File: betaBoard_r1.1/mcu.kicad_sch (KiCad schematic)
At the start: 27 parts, among them SW1 C26638, SW2 C26638, U2 W25Q128JVSIQ, U3 RP2040, Y1 X322512MSB4SI

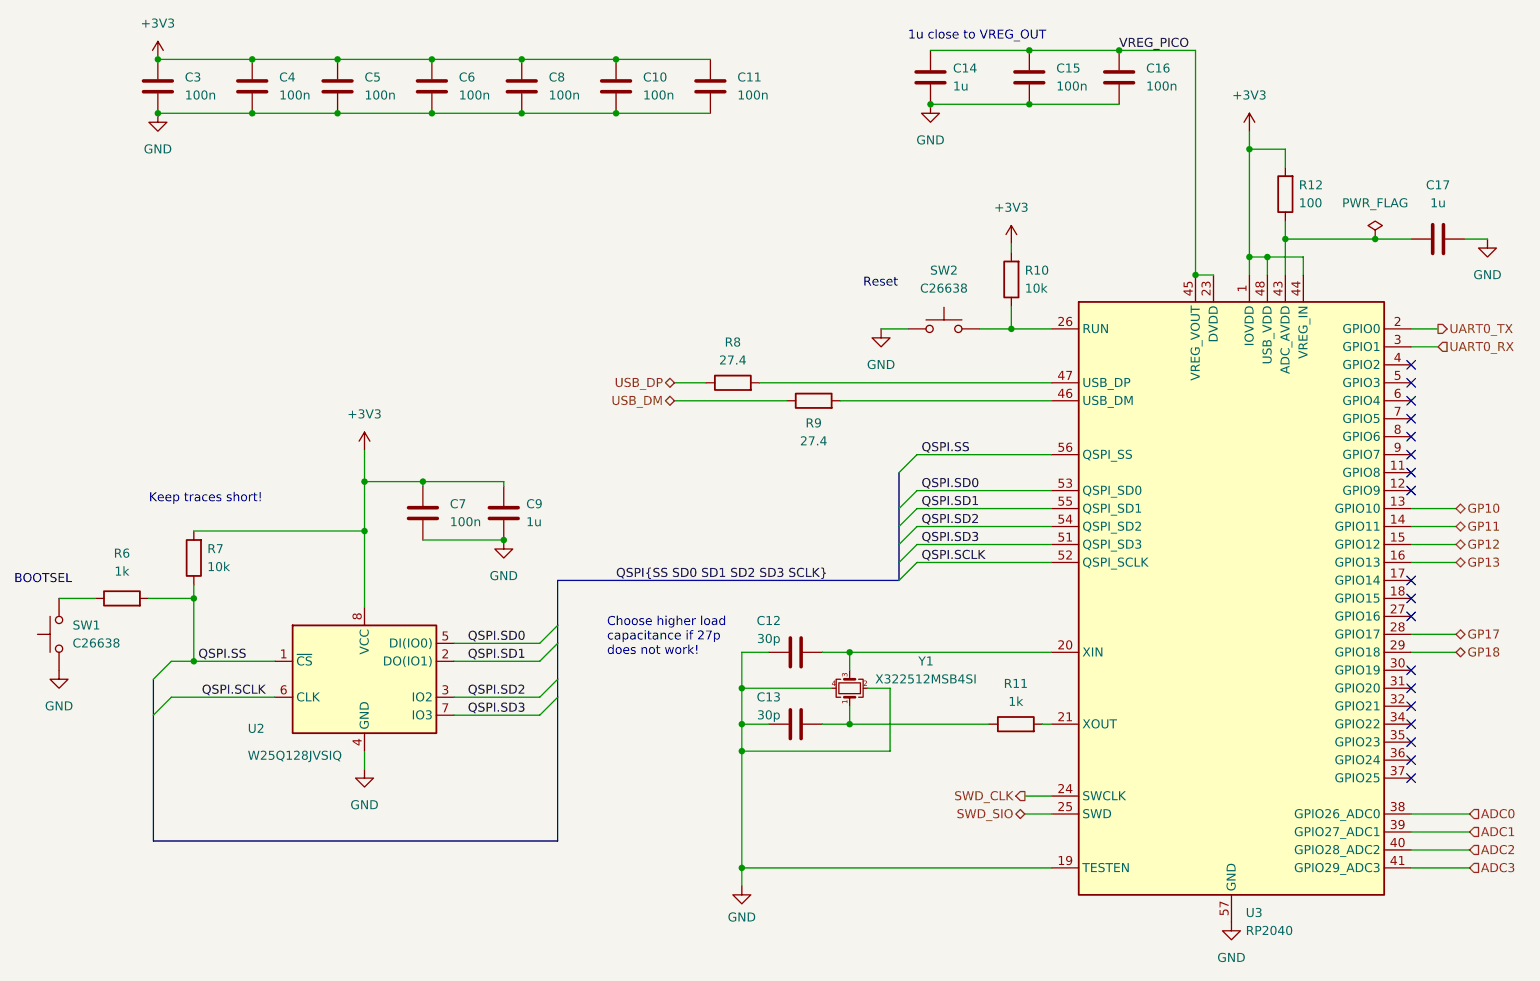
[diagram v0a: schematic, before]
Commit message: move all hardware files to one folder
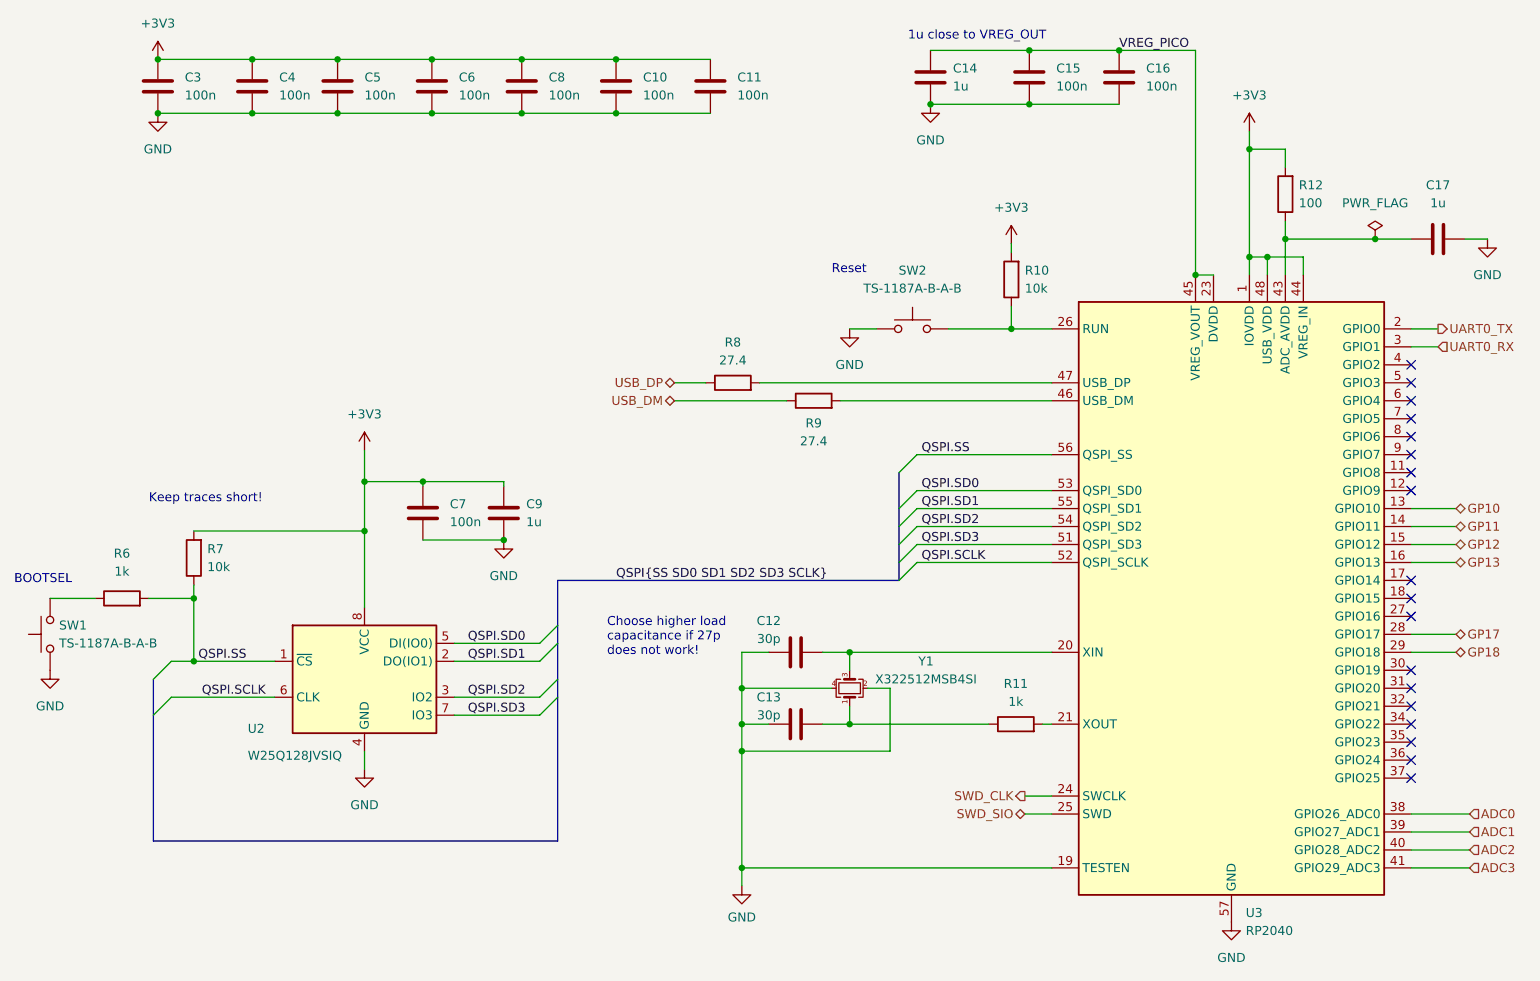
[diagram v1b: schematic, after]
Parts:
- SW1, SW2: value C26638 -> TS-1187A-B-A-B
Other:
- moved on the sheet: SW1, SW2
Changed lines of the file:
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@@
     (title "Beta Board")
     (date "2023-12-28")
-    (rev "R1.0")
+    (rev "R1.1")
     (company "Tim Kuhlbusch")
     (comment 1 "Beta radiation detector")
@@
     (stroke (width 0) (type default))
   )
-  (wire (pts (xy 141.605 71.12) (xy 145.415 71.12))
+  (wire (pts (xy 137.16 71.12) (xy 140.97 71.12))
     (stroke (width 0) (type default))
   )
@@
     (stroke (width 0) (type default))
   )
-  (wire (pts (xy 155.575 71.12) (xy 160.02 71.12))
+  (wire (pts (xy 151.13 71.12) (xy 160.02 71.12))
     (stroke (width 0) (type default))
   )
@@
     (stroke (width 0) (type default))
   )
-  (wire (pts (xy 25.4 109.22) (xy 30.48 109.22))
+  (wire (pts (xy 24.13 109.22) (xy 30.48 109.22))
     (stroke (width 0) (type default))
   )
@@
     (effects (font (size 1.27 1.27)) (justify left bottom))
   )
-  (text "Reset\n" (at 139.065 65.405 0)
+  (text "Reset\n" (at 134.62 63.5 0)
     (effects (font (size 1.27 1.27)) (justify left bottom))
   )
@@
     )
   )
-  (symbol (lib_id "power:GND") (at 141.605 71.12 0) (unit 1)
-    (in_bom yes) (on_board yes) (dnp no) (fields_autoplaced)
-    (property "Reference" "#PWR023" (at 141.605 77.47 0)
-      (effects (font (size 1.27 1.27)) hide)
-    )
-    (property "Value" "GND" (at 141.605 76.2 0)
-      (effects (font (size 1.27 1.27)))
-    )
-    (property "Footprint" "" (at 141.605 71.12 0)
-      (effects (font (size 1.27 1.27)) hide)
-    )
-    (property "Datasheet" "" (at 141.605 71.12 0)
+  (symbol (lib_id "power:GND") (at 137.16 71.12 0) (unit 1)
+    (in_bom yes) (on_board yes) (dnp no) (fields_autoplaced)
+    (property "Reference" "#PWR023" (at 137.16 77.47 0)
+      (effects (font (size 1.27 1.27)) hide)
+    )
+    (property "Value" "GND" (at 137.16 76.2 0)
+      (effects (font (size 1.27 1.27)))
+    )
+    (property "Footprint" "" (at 137.16 71.12 0)
+      (effects (font (size 1.27 1.27)) hide)
+    )
+    (property "Datasheet" "" (at 137.16 71.12 0)
       (effects (font (size 1.27 1.27)) hide)
     )
@@
     )
   )
-  (symbol (lib_id "power:GND") (at 25.4 119.38 0) (unit 1)
-    (in_bom yes) (on_board yes) (dnp no) (fields_autoplaced)
-    (property "Reference" "#PWR016" (at 25.4 125.73 0)
-      (effects (font (size 1.27 1.27)) hide)
-    )
-    (property "Value" "GND" (at 25.4 124.46 0)
-      (effects (font (size 1.27 1.27)))
-    )
-    (property "Footprint" "" (at 25.4 119.38 0)
-      (effects (font (size 1.27 1.27)) hide)
-    )
-    (property "Datasheet" "" (at 25.4 119.38 0)
+  (symbol (lib_id "power:GND") (at 24.13 119.38 0) (unit 1)
+    (in_bom yes) (on_board yes) (dnp no) (fields_autoplaced)
+    (property "Reference" "#PWR016" (at 24.13 125.73 0)
+      (effects (font (size 1.27 1.27)) hide)
+    )
+    (property "Value" "GND" (at 24.13 124.46 0)
+      (effects (font (size 1.27 1.27)))
+    )
+    (property "Footprint" "" (at 24.13 119.38 0)
+      (effects (font (size 1.27 1.27)) hide)
+    )
+    (property "Datasheet" "" (at 24.13 119.38 0)
       (effects (font (size 1.27 1.27)) hide)
     )
@@
     )
   )
-  (symbol (lib_id "Switch:SW_Push") (at 150.495 71.12 0) (unit 1)
-    (in_bom yes) (on_board yes) (dnp no) (fields_autoplaced)
-    (property "Reference" "SW2" (at 150.495 62.865 0)
-      (effects (font (size 1.27 1.27)))
-    )
-    (property "Value" "C26638" (at 150.495 65.405 0)
-      (effects (font (size 1.27 1.27)))
-    )
-    (property "Footprint" "betaBoard:TS-1187A-B-A-B" (at 150.495 66.04 0)
-      (effects (font (size 1.27 1.27)) hide)
-    )
-    (property "Datasheet" "~" (at 150.495 66.04 0)
+  (symbol (lib_id "Switch:SW_Push") (at 146.05 71.12 0) (unit 1)
+    (in_bom yes) (on_board yes) (dnp no) (fields_autoplaced)
+    (property "Reference" "SW2" (at 146.05 62.865 0)
+      (effects (font (size 1.27 1.27)))
+    )
+    (property "Value" "TS-1187A-B-A-B" (at 146.05 65.405 0)
+      (effects (font (size 1.27 1.27)))
+    )
+    (property "Footprint" "betaBoard:TS-1187A-B-A-B" (at 146.05 66.04 0)
+      (effects (font (size 1.27 1.27)) hide)
+    )
+    (property "Datasheet" "~" (at 146.05 66.04 0)
       (effects (font (size 1.27 1.27)) hide)
     )
@@
     )
   )
-  (symbol (lib_id "Switch:SW_Push") (at 25.4 114.3 90) (unit 1)
-    (in_bom yes) (on_board yes) (dnp no) (fields_autoplaced)
-    (property "Reference" "SW1" (at 27.305 113.0299 90)
+  (symbol (lib_id "Switch:SW_Push") (at 24.13 114.3 90) (unit 1)
+    (in_bom yes) (on_board yes) (dnp no) (fields_autoplaced)
+    (property "Reference" "SW1" (at 25.4 113.03 90)
       (effects (font (size 1.27 1.27)) (justify right))
     )
-    (property "Value" "C26638" (at 27.305 115.5699 90)
+    (property "Value" "TS-1187A-B-A-B\n" (at 25.4 115.57 90)
       (effects (font (size 1.27 1.27)) (justify right))
     )
-    (property "Footprint" "betaBoard:TS-1187A-B-A-B" (at 20.32 114.3 0)
-      (effects (font (size 1.27 1.27)) hide)
-    )
-    (property "Datasheet" "~" (at 20.32 114.3 0)
-      (effects (font (size 1.27 1.27)) hide)
-    )
+    (property "Footprint" "betaBoard:TS-1187A-B-A-B" (at 19.05 114.3 0)
+      (effects (font (size 1.27 1.27)) hide)
+    )
+    (property "Datasheet" "~" (at 19.05 114.3 0)
+      (effects (font (size 1.27 1.27)) hide)
+    )
